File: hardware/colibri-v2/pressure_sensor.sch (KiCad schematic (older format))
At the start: 6 parts

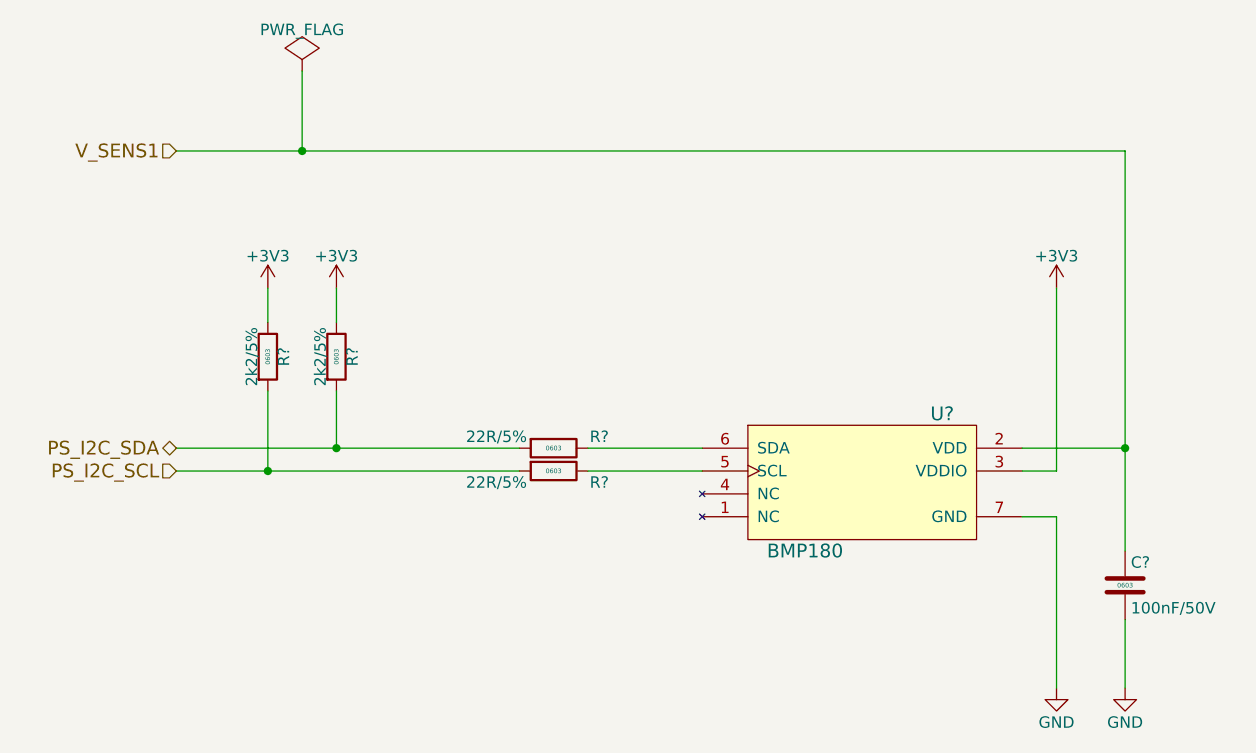
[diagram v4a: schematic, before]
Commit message: Resolving ERC problems
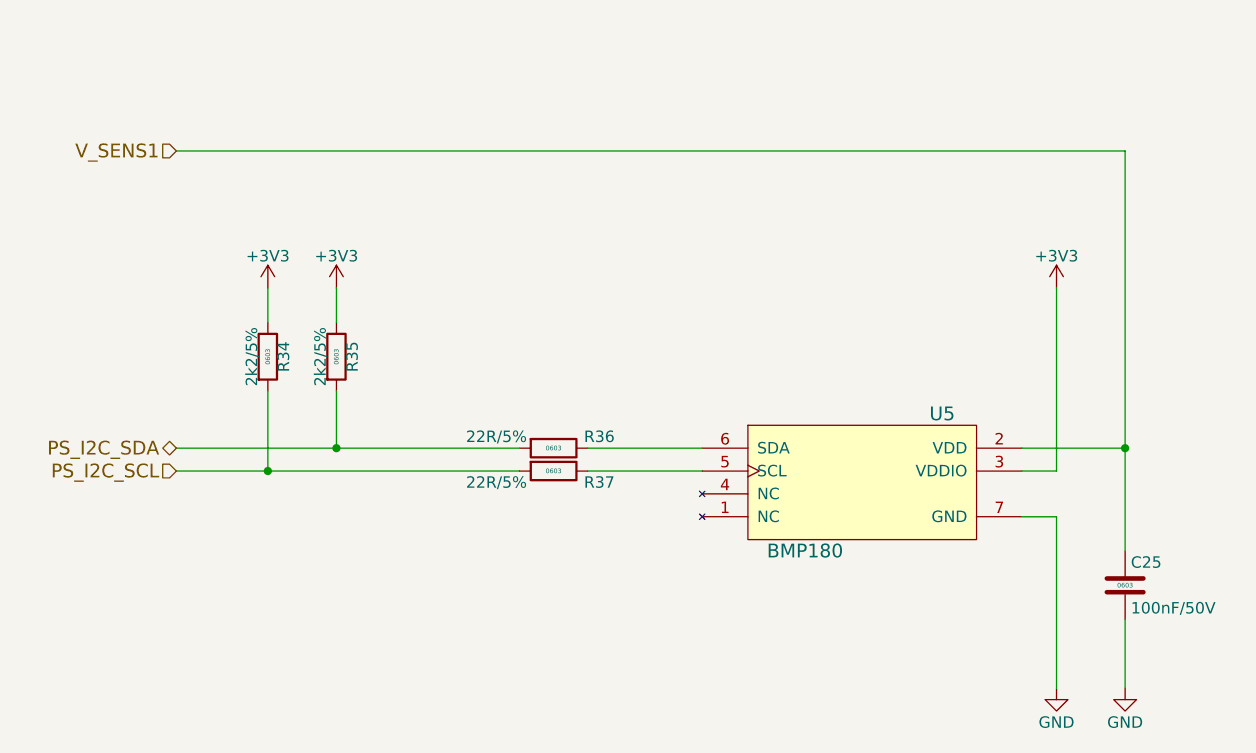
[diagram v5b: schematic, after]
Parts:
- gave numbers to parts that had none: 6
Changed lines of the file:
@@
 EESchema Schematic File Version 2
+LIBS:colibri-wnd-rescue
 LIBS:power
 LIBS:device
@@
 $EndDescr
 $Comp
-L BMP180 U?
+L BMP180 U5
 U 1 1 558FDE4B
 P 5950 3650
-F 0 "U?" H 6300 3950 60  0000 C CNN
+F 0 "U5" H 6300 3950 60  0000 C CNN
 F 1 "BMP180" H 5700 3350 60  0000 C CNN
 F 2 "" H 5950 3650 60  0001 C CNN
@@
 	4750 3600 5250 3600
 $Comp
-L +3V3 #PWR?
+L +3V3 #PWR044
 U 1 1 558FDF78
 P 3350 2800
-F 0 "#PWR?" H 3350 2650 50  0001 C CNN
+F 0 "#PWR044" H 3350 2650 50  0001 C CNN
 F 1 "+3V3" H 3350 2940 50  0000 C CNN
 F 2 "" H 3350 2800 60  0000 C CNN
@@
 $EndComp
 $Comp
-L +3V3 #PWR?
+L +3V3 #PWR045
 U 1 1 558FDF8F
 P 3650 2800
-F 0 "#PWR?" H 3650 2650 50  0001 C CNN
+F 0 "#PWR045" H 3650 2650 50  0001 C CNN
 F 1 "+3V3" H 3650 2940 50  0000 C CNN
 F 2 "" H 3650 2800 60  0000 C CNN
@@
 Connection ~ 7100 3500
 $Comp
-L GND #PWR?
+L GND #PWR046
 U 1 1 558FE2F6
 P 7100 4550
-F 0 "#PWR?" H 7100 4300 50  0001 C CNN
+F 0 "#PWR046" H 7100 4300 50  0001 C CNN
 F 1 "GND" H 7100 4400 50  0000 C CNN
 F 2 "" H 7100 4550 60  0000 C CNN
@@
 $EndComp
 $Comp
-L GND #PWR?
+L GND #PWR047
 U 1 1 558FE312
 P 6800 4550
-F 0 "#PWR?" H 6800 4300 50  0001 C CNN
+F 0 "#PWR047" H 6800 4300 50  0001 C CNN
 F 1 "GND" H 6800 4400 50  0000 C CNN
 F 2 "" H 6800 4550 60  0000 C CNN
@@
 	7100 2200 7100 3950
 $Comp
-L PWR_FLAG #FLG?
-U 1 1 55FF4C0A
-P 3500 1850
-F 0 "#FLG?" H 3500 1945 50  0001 C CNN
-F 1 "PWR_FLAG" H 3500 2030 50  0000 C CNN
-F 2 "" H 3500 1850 60  0000 C CNN
-F 3 "" H 3500 1850 60  0000 C CNN
-	1    3500 1850
-	1    0    0    -1
-$EndComp
-Wire Wire Line
-	3500 1850 3500 2200
-Connection ~ 3500 2200
-$Comp
-L +3V3 #PWR?
+L +3V3 #PWR048
 U 1 1 562303A9
 P 6800 2800
-F 0 "#PWR?" H 6800 2650 50  0001 C CNN
+F 0 "#PWR048" H 6800 2650 50  0001 C CNN
 F 1 "+3V3" H 6800 2940 50  0000 C CNN
 F 2 "" H 6800 2800 60  0000 C CNN
@@
 	6800 3600 6800 2800
 $Comp
-L R_SMT R?
+L R_SMT R35
 U 1 1 562F15F5
 P 3650 3100
-F 0 "R?" V 3720 3100 50  0000 C CNN
+F 0 "R35" V 3720 3100 50  0000 C CNN
 F 1 "2k2/5%" V 3580 3100 50  0000 C CNN
 F 2 "Resistors_SMD:R_0603" V 3800 3100 30  0001 C CNN
@@
 $EndComp
 $Comp
-L R_SMT R?
+L R_SMT R34
 U 1 1 562F1678
 P 3350 3100
-F 0 "R?" V 3420 3100 50  0000 C CNN
+F 0 "R34" V 3420 3100 50  0000 C CNN
 F 1 "2k2/5%" V 3280 3100 50  0000 C CNN
 F 2 "Resistors_SMD:R_0603" V 3500 3100 30  0001 C CNN
@@
 $EndComp
 $Comp
-L R_SMT R?
+L R_SMT R36
 U 1 1 562F16F0
 P 4600 3500
-F 0 "R?" V 4550 3700 50  0000 C CNN
+F 0 "R36" V 4550 3700 50  0000 C CNN
 F 1 "22R/5%" V 4550 3250 50  0000 C CNN
 F 2 "Resistors_SMD:R_0603" V 4750 3500 30  0001 C CNN
@@
 $EndComp
 $Comp
-L R_SMT R?
+L R_SMT R37
 U 1 1 562F17F9
 P 4600 3600
-F 0 "R?" V 4650 3800 50  0000 C CNN
+F 0 "R37" V 4650 3800 50  0000 C CNN
 F 1 "22R/5%" V 4650 3350 50  0000 C CNN
 F 2 "Resistors_SMD:R_0603" V 4750 3600 30  0001 C CNN
@@
 $EndComp
 $Comp
-L C_SMT C?
+L C_SMT C25
 U 1 1 562F2485
 P 7100 4100
-F 0 "C?" H 7125 4200 50  0000 L CNN
+F 0 "C25" H 7125 4200 50  0000 L CNN
 F 1 "100nF/50V" H 7125 4000 50  0000 L CNN
 F 2 "Capacitors_SMD:C_0603" H 7130 3950 30  0001 L CNN
